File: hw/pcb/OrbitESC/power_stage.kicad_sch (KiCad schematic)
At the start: 37 parts, among them U5 DRV8300DRGER, U6 TSV994

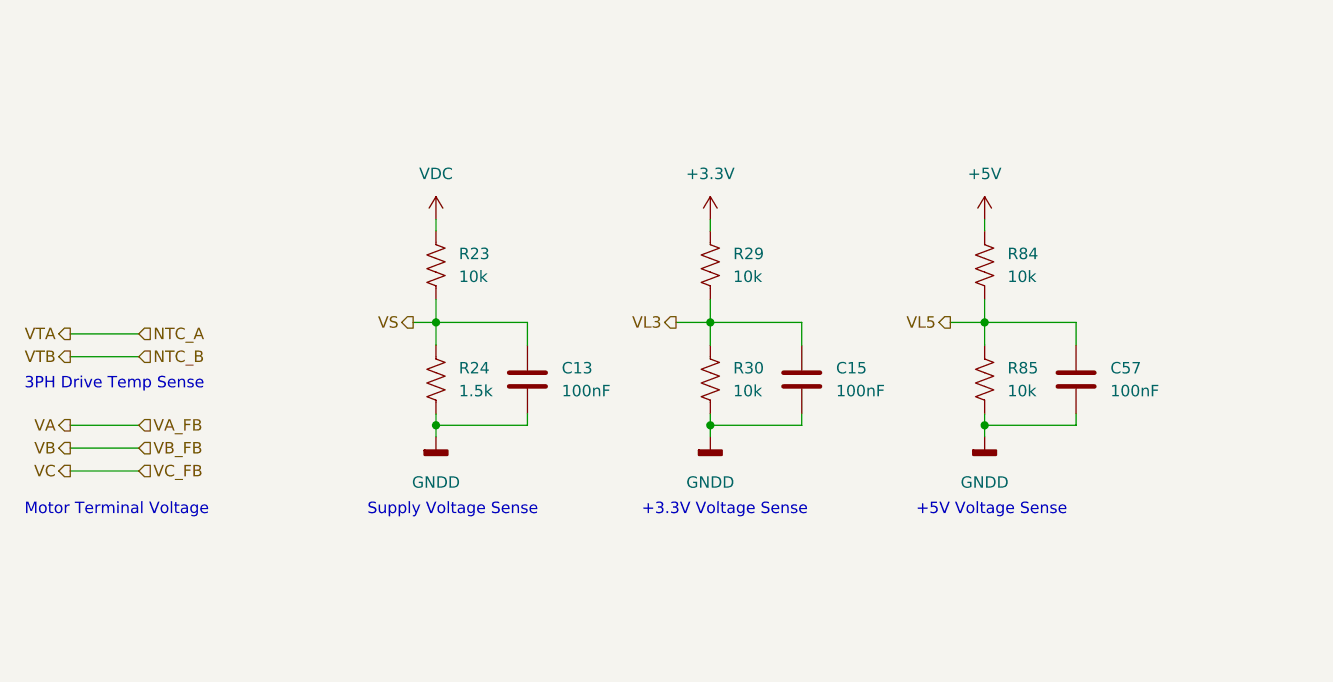
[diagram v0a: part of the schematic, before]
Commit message: Start rework of processor selection after realizing I can't afford manufacturing...
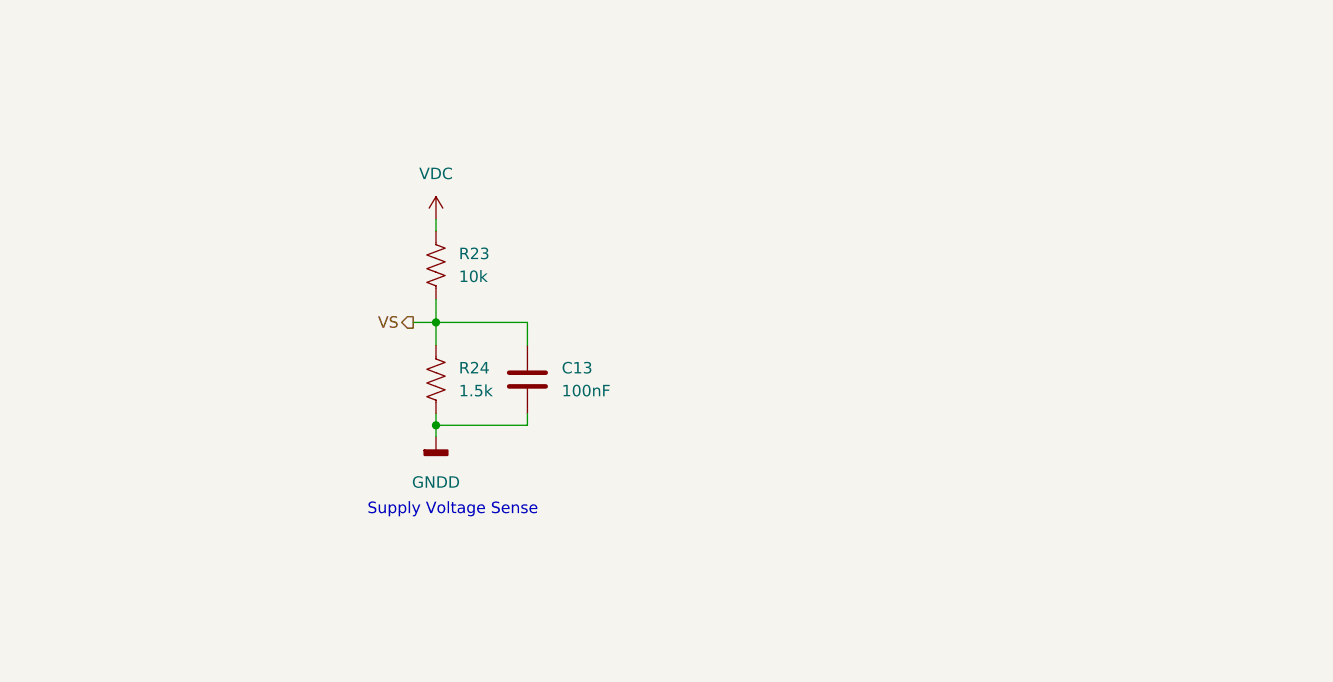
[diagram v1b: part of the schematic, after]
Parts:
- removed C15, C57: 100nF, Capacitor_SMD:C_0402_1005Metric, symbol Device:C
- removed R29, R30, R84, R85: 10k, Resistor_SMD:R_0402_1005Metric, symbol Device:R_US
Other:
- note removed: "+3.3V Voltage Sense"
- note removed: "+5V Voltage Sense"
- note removed: "3PH Drive Temp Sense"
- note removed: "Motor Terminal Voltage"

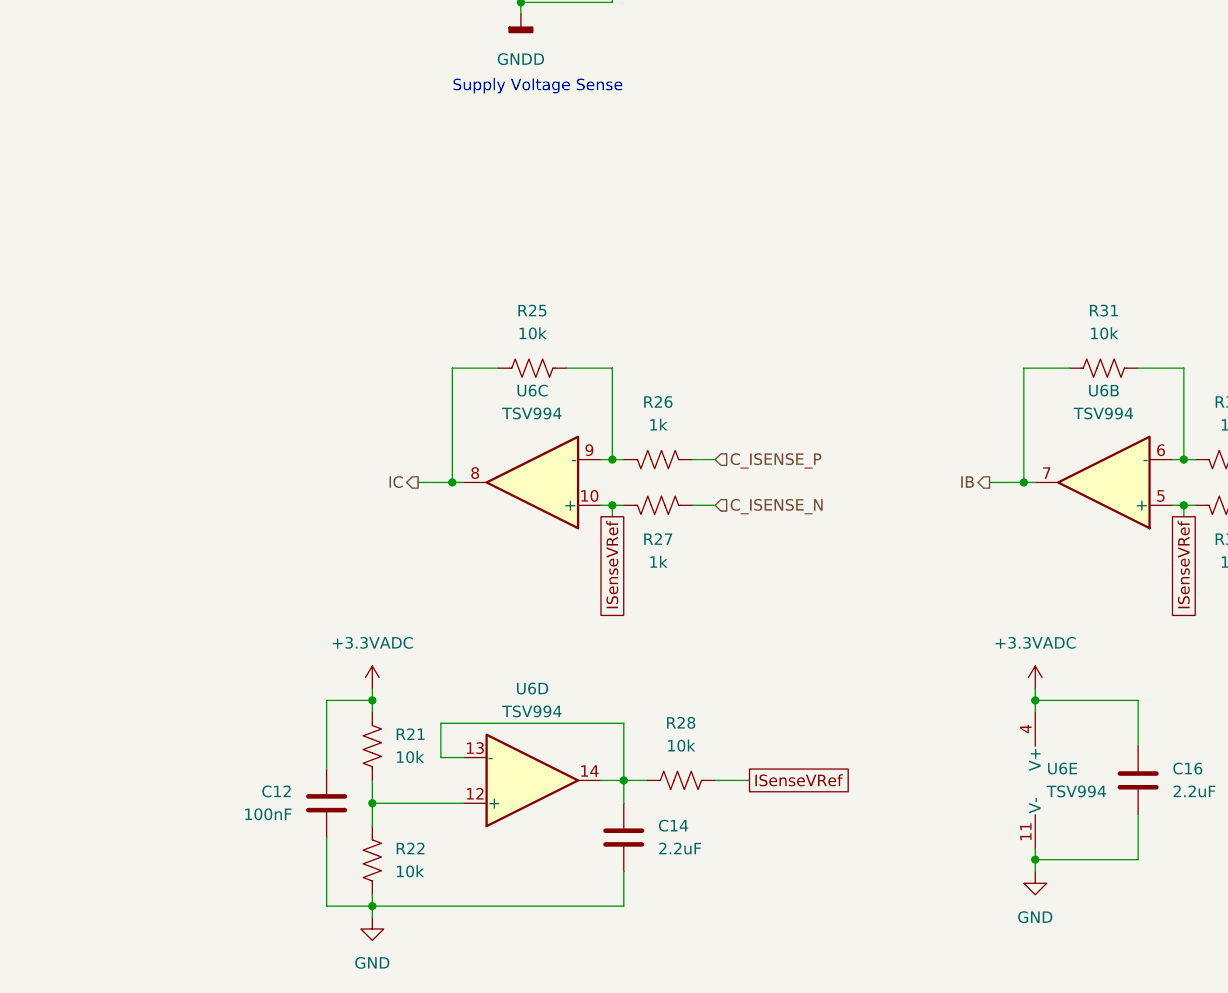
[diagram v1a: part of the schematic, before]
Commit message: Start adding simulation for analog
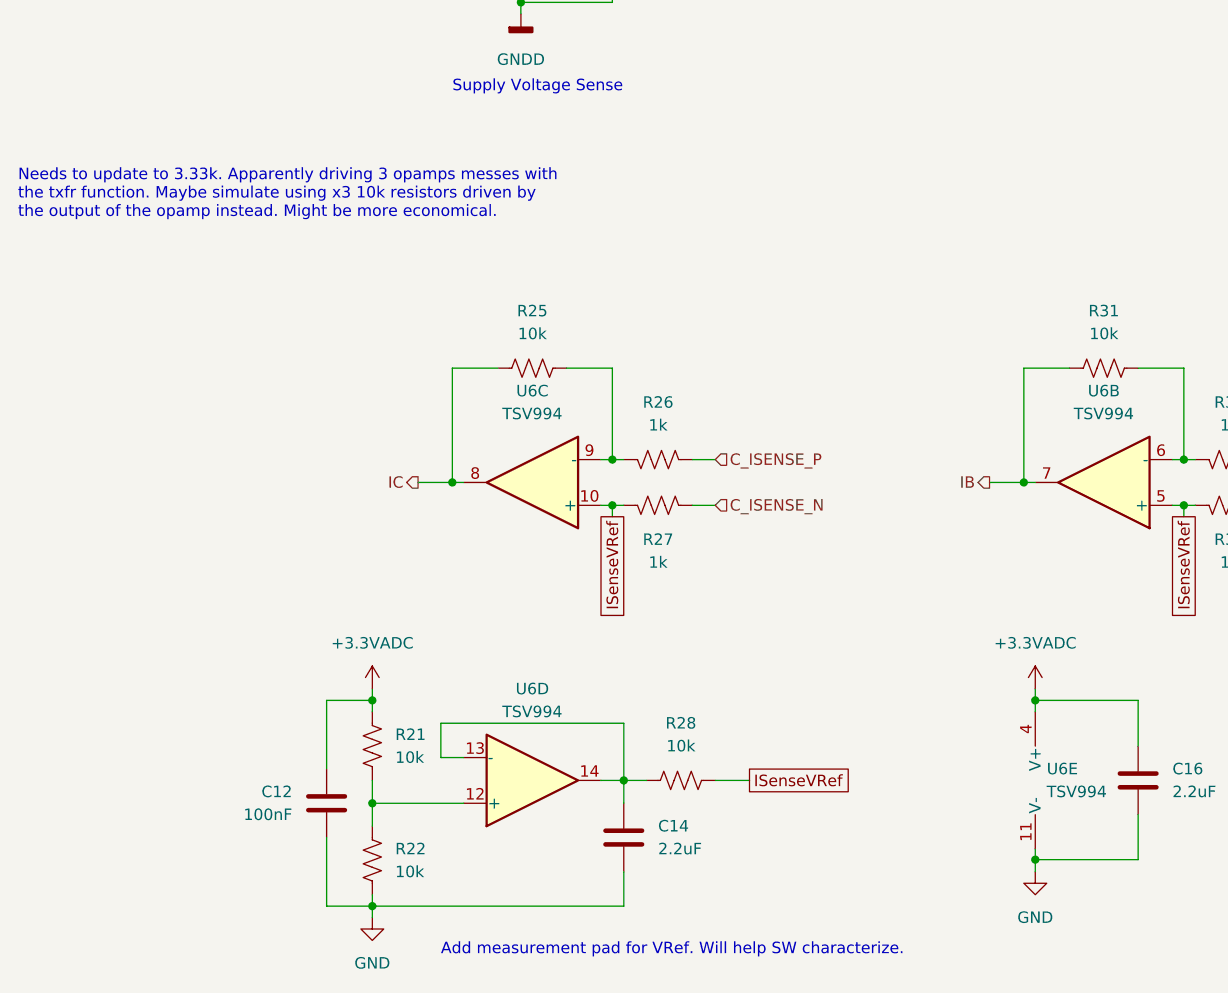
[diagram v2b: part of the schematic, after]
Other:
- note added: "Add measurement pad for VRef. Will help SW characterize."
- note added: "Needs to update to 3.33k. Apparently driving 3 opamps messes with the txfr function. Maybe simulate using x3 10k resistors driven by the output of the opamp instead. Might be more economical."
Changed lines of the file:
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@@
     (stroke (width 0) (type default) (color 0 0 0 0))
+  )
+  (text "Needs to update to 3.33k. Apparently driving 3 opamps messes with\nthe txfr function. Maybe simulate using x3 10k resistors driven by\nthe output of the opamp instead. Might be more economical."
+    (at 21.59 111.76 0)
+    (effects (font (size 1.27 1.27)) (justify left bottom))
   )
   (text "Supply Voltage Sense" (at 69.85 97.79 0)
     (effects (font (size 1.27 1.27)) (justify left bottom))
   )
+  (text "Add measurement pad for VRef. Will help SW characterize."
+    (at 68.58 193.675 0)
+    (effects (font (size 1.27 1.27)) (justify left bottom))
+  )

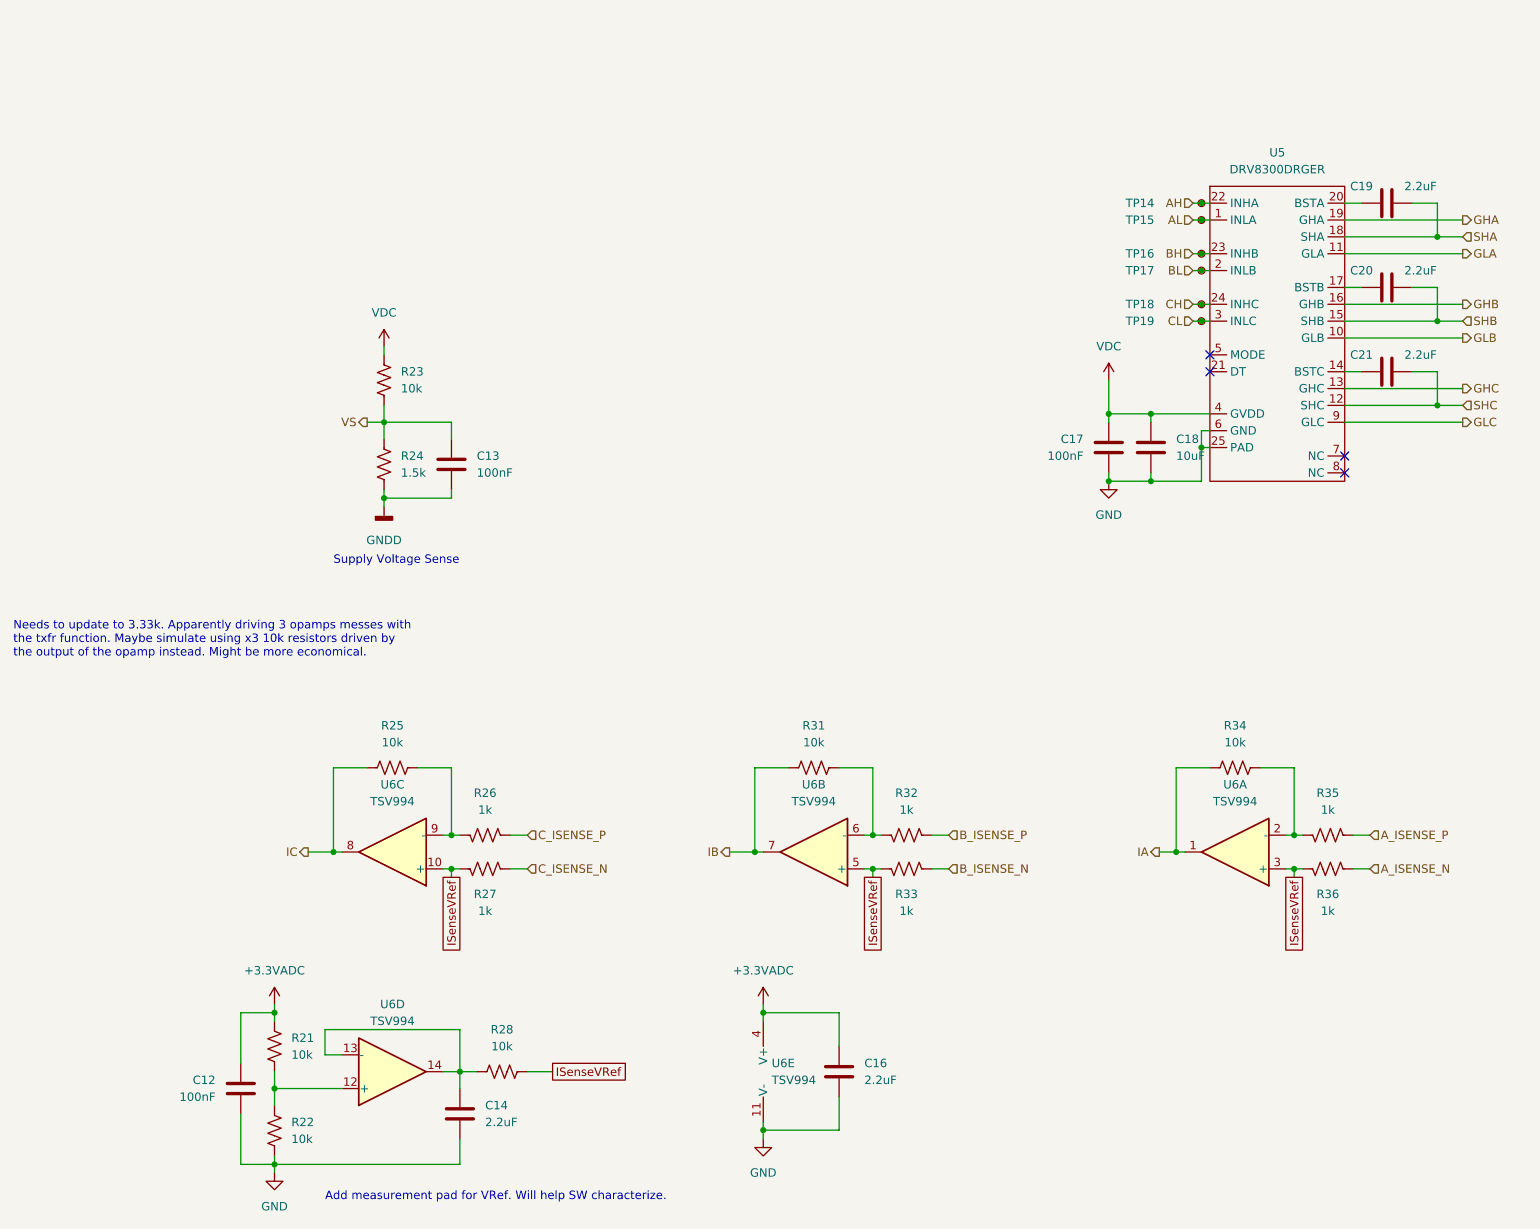
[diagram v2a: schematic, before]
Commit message: Update a few issues with the analog and power stage
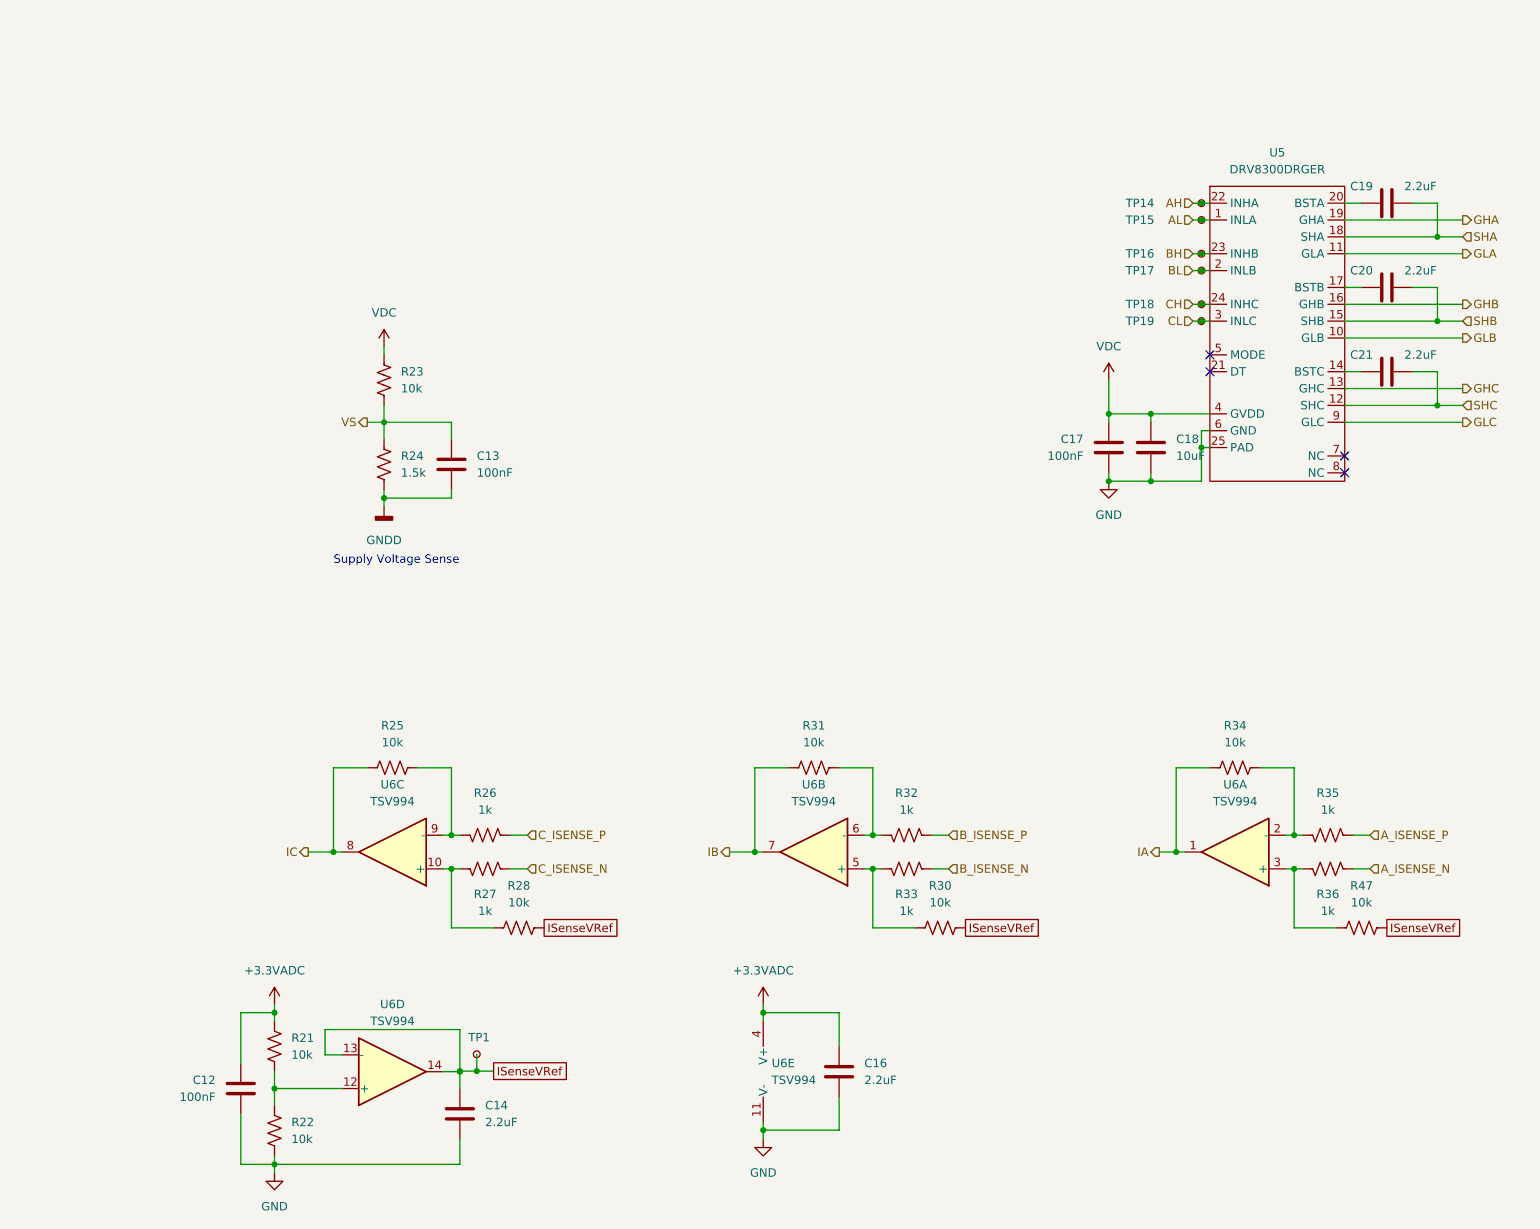
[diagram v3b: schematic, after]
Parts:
- added R30, R47: 10k, Resistor_SMD:R_0402_1005Metric, symbol Device:R_US
- added TP1: BL, TestPoint:TestPoint_Pad_D1.0mm, symbol Connector:TestPoint_Small
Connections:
- net ISenseVRef: now also C14.1, U6.13 (-), U6.14, R30.2, R47.2, TP1.1; no longer R27.2, R33.2, R36.2, U6.10 (+), U6.3 (+), U6.5 (+)
- new net: R36.2, R47.1, U6.3 (+)
- new net: R27.2, R28.1, U6.10 (+)
- new net: R30.1, R33.2, U6.5 (+)
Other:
- note removed: "Add measurement pad for VRef. Will help SW characterize."
- note removed: "Needs to update to 3.33k. Apparently driving 3 opamps messes with the txfr function. Maybe simulate using x3 10k resistors driven by the output of the opamp instead. Might be more economical."
- moved on the sheet: R28

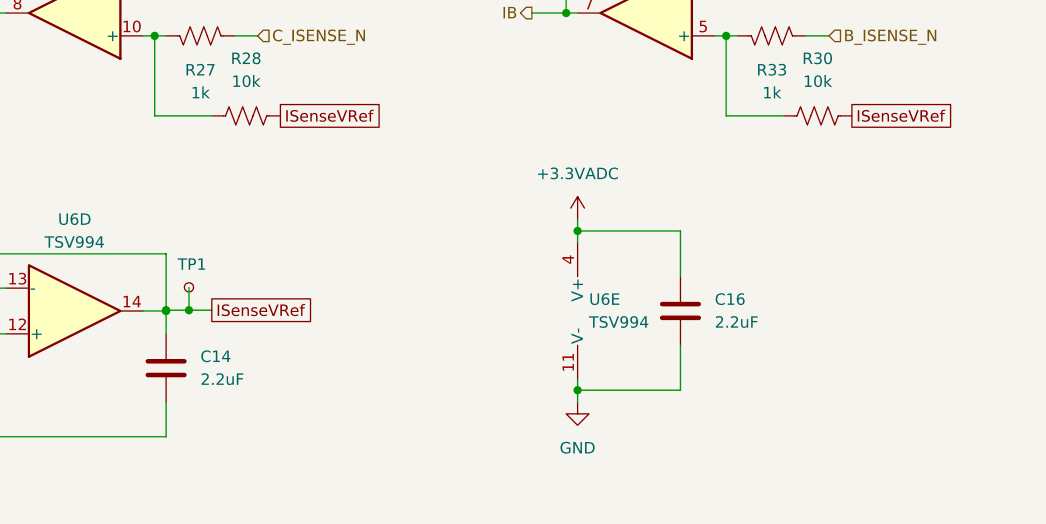
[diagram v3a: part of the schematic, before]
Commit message: Schematic corrections
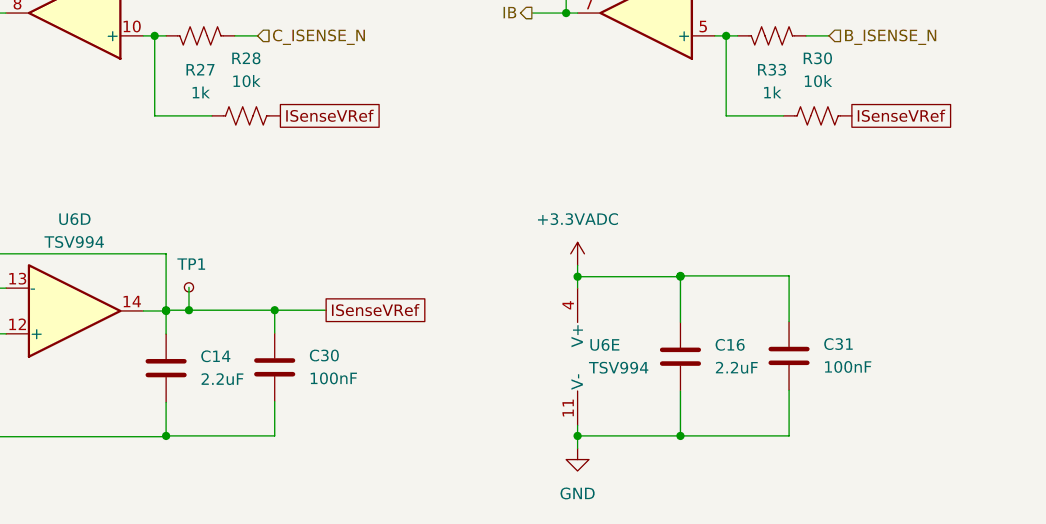
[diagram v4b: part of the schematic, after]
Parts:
- added C30, C31: 100nF, Capacitor_SMD:C_0402_1005Metric, symbol Device:C
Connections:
- net GND: now also C30.2, C31.2
- net ISenseVRef: now also C30.1
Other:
- moved on the sheet: C16, U6E

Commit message: Sync lunch schematic update
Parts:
- removed C16: 2.2uF, Capacitor_SMD:C_0805_2012Metric, symbol Device:C
- removed C31: 100nF, Capacitor_SMD:C_0402_1005Metric, symbol Device:C
- removed U6: TSV994, Package_SO:TSSOP-14_4.4x5mm_P0.65mm, symbol Amplifier_Operational:TSV994
- added C? (x4): 100nF, Capacitor_SMD:C_0402_1005Metric, symbol Device:C
- added U? (x4): TLV9051IDBVR, Package_TO_SOT_SMD:SOT-23-5, symbol Amplifier_Operational:TLV9001IDCK
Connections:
- net +3.3VADC: now also C?.1, C?.1, C?.1, C?.1, U?.5 (V+), U?.5 (V+), U?.5 (V+), U?.5 (V+)
- net GND: now also C?.2, C?.2, C?.2, C?.2, U?.4 (V-), U?.4 (V-), U?.4 (V-), U?.4 (V-)
- net IA: now also U?.1
- net IB: now also U?.1
- net IC: now also U?.1
- net ISenseVRef: now also U?.1; no longer C14.1
- net at R36.2, R47.1: now also U?.3 (+)
- net at R25.2, R26.2: now also U?.2 (-)
- net at R21.1, R22.2: now also U?.3 (+)
- net at R27.2, R28.1: now also U?.3 (+)
- net at R34.2, R35.2: now also U?.2 (-)
- net at R31.2, R32.2: now also U?.2 (-)
- net at R30.1, R33.2: now also U?.3 (+)
